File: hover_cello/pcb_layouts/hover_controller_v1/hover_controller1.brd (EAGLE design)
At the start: 160 x 100 mm, 6 parts

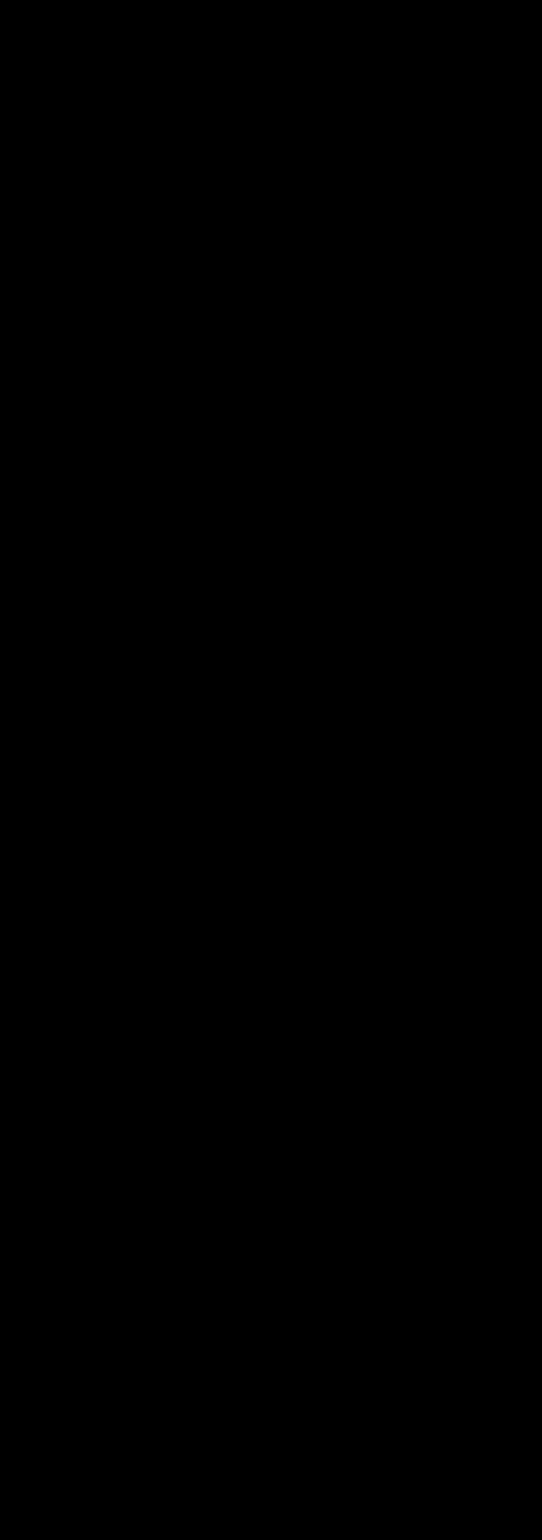
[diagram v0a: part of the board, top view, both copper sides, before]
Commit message: fixed annoying line not found bug, added delay on startup
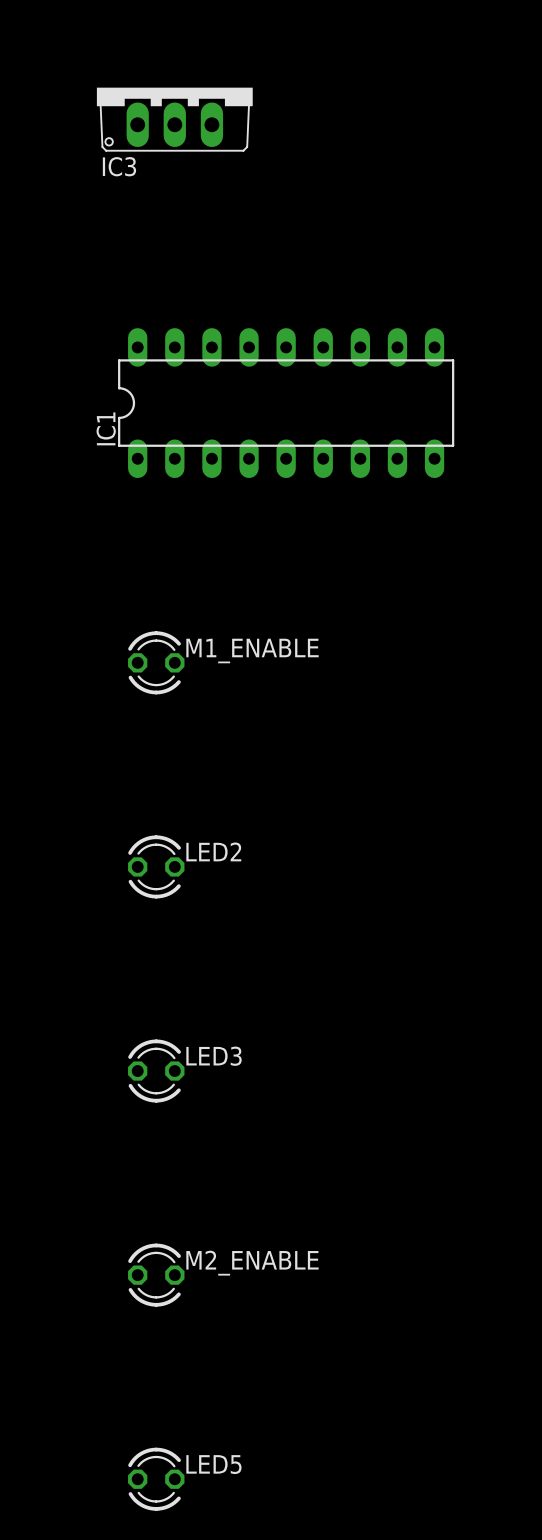
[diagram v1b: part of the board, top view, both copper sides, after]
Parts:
- added IC1: (no value), uln-udn:DIL18
- added IC3: 7805TV, linear:TO220V
- added LED2, LED3, LED5, M1_ENABLE, M2_ENABLE: (no value), led:LED3MM
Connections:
- new net N$3: LED3.K, M2_ENABLE.K
- new net N$4: LED3.A, M2_ENABLE.A
- net GND: now also IC1.9
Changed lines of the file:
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@@
 <element name="J1" library="jumper" package="SJW" value="" x="12.7" y="48.26" rot="R270"/>
 <element name="J2" library="jumper" package="SJW" value="" x="26.67" y="48.26" rot="R270"/>
+<element name="IC3" library="linear" package="TO220V" value="7805TV" x="10.16" y="-49.53"/>
+<element name="IC1" library="uln-udn" library_urn="urn:adsk.eagle:library:407" package="DIL18" value="" x="17.78" y="-71.12"/>
+<element name="M1_ENABLE" library="led" library_urn="urn:adsk.eagle:library:259" package="LED3MM" value="" x="8.89" y="-88.9"/>
+<element name="LED2" library="led" library_urn="urn:adsk.eagle:library:259" package="LED3MM" value="" x="8.89" y="-102.87"/>
+<element name="LED3" library="led" library_urn="urn:adsk.eagle:library:259" package="LED3MM" value="" x="8.89" y="-116.84"/>
+<element name="M2_ENABLE" library="led" library_urn="urn:adsk.eagle:library:259" package="LED3MM" value="" x="8.89" y="-130.81"/>
+<element name="LED5" library="led" library_urn="urn:adsk.eagle:library:259" package="LED3MM" value="" x="8.89" y="-144.78"/>
 </elements>
 <signals>
@@
 <contactref element="MOTOR2" pad="1"/>
 <contactref element="MOTOR1" pad="1"/>
+<contactref element="IC1" pad="9"/>
 <wire x1="12.7" y1="54.61" x2="26.67" y2="54.61" width="0" layer="19" extent="1-1"/>
 <wire x1="26.67" y1="34.671" x2="26.67" y2="54.61" width="0" layer="19" extent="1-1"/>
 <wire x1="39.37" y1="29.21" x2="26.67" y2="34.671" width="0" layer="19" extent="1-1"/>
 <wire x1="41.91" y1="29.21" x2="39.37" y2="29.21" width="0" layer="19" extent="1-1"/>
+<wire x1="27.94" y1="-74.93" x2="39.37" y2="29.21" width="0" layer="19" extent="1-1"/>
 </signal>
 <signal name="USB">
@@
 <wire x1="26.67" y1="24.511" x2="26.67" y2="59.69" width="0" layer="19" extent="1-1"/>
 </signal>
+<signal name="N$3">
+<contactref element="M2_ENABLE" pad="K"/>
+<contactref element="LED3" pad="K"/>
+<wire x1="10.16" y1="-116.84" x2="10.16" y2="-130.81" width="0" layer="19" extent="1-1"/>
+</signal>
+<signal name="N$4">
+<contactref element="M2_ENABLE" pad="A"/>
+<contactref element="LED3" pad="A"/>
+<wire x1="7.62" y1="-116.84" x2="7.62" y2="-130.81" width="0" layer="19" extent="1-1"/>
+</signal>
 </signals>
 </board>
 </drawing>
+<compatibility>
+<note version="8.2" severity="warning">
+Since Version 8.2, Eagle supports online libraries. The ids
+of those online libraries will not be understood (or retained)
+with this version.
+</note>
+</compatibility>
 </eagle>

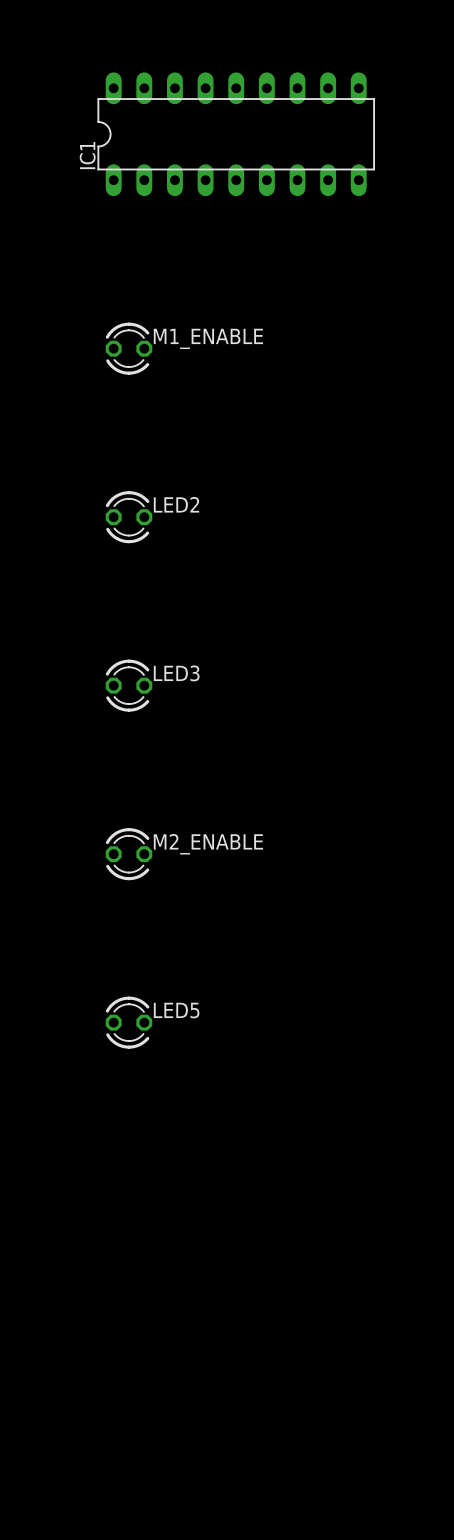
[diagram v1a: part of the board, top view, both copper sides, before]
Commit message: added L298 DC motor driver to Eagle schematic
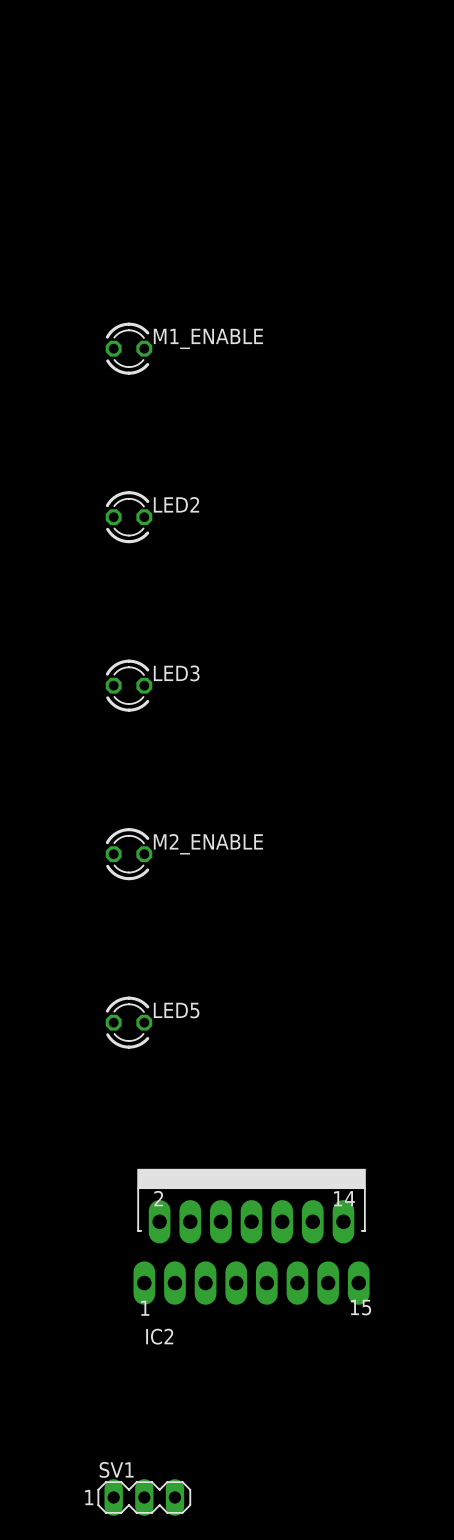
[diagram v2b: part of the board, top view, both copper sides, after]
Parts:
- removed IC1: (no value), uln-udn:DIL18
- added IC2: L298, st-microelectronics:MULTIWATT-15
- added SV1: (no value), con-lstb:MA03-1
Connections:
- new net VS: IC2.4
- net GND: now also IC2.8; no longer IC1.9
- net VCC: now also IC2.9
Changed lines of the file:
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@@
 <element name="J2" library="jumper" package="SJW" value="" x="26.67" y="48.26" rot="R270"/>
 <element name="IC3" library="linear" package="TO220V" value="7805TV" x="10.16" y="-49.53"/>
-<element name="IC1" library="uln-udn" library_urn="urn:adsk.eagle:library:407" package="DIL18" value="" x="17.78" y="-71.12"/>
 <element name="M1_ENABLE" library="led" library_urn="urn:adsk.eagle:library:259" package="LED3MM" value="" x="8.89" y="-88.9"/>
 <element name="LED2" library="led" library_urn="urn:adsk.eagle:library:259" package="LED3MM" value="" x="8.89" y="-102.87"/>
@@
 <element name="M2_ENABLE" library="led" library_urn="urn:adsk.eagle:library:259" package="LED3MM" value="" x="8.89" y="-130.81"/>
 <element name="LED5" library="led" library_urn="urn:adsk.eagle:library:259" package="LED3MM" value="" x="8.89" y="-144.78"/>
+<element name="IC2" library="st-microelectronics" package="MULTIWATT-15" value="L298" x="19.05" y="-158.75">
+<attribute name="MF" value="" x="19.05" y="-158.75" size="1.778" layer="27" display="off"/>
+<attribute name="MPN" value="L298N" x="19.05" y="-158.75" size="1.778" layer="27" display="off"/>
+<attribute name="OC_FARNELL" value="1589425" x="19.05" y="-158.75" size="1.778" layer="27" display="off"/>
+<attribute name="OC_NEWARK" value="32M1527" x="19.05" y="-158.75" size="1.778" layer="27" display="off"/>
+</element>
+<element name="SV1" library="con-lstb" package="MA03-1" value="" x="10.16" y="-184.15">
+<attribute name="MF" value="" x="10.16" y="-184.15" size="1.778" layer="27" display="off"/>
+<attribute name="MPN" value="" x="10.16" y="-184.15" size="1.778" layer="27" display="off"/>
+<attribute name="OC_FARNELL" value="unknown" x="10.16" y="-184.15" size="1.778" layer="27" display="off"/>
+<attribute name="OC_NEWARK" value="unknown" x="10.16" y="-184.15" size="1.778" layer="27" display="off"/>
+</element>
 </elements>
 <signals>
@@
 <contactref element="MOTOR2" pad="1"/>
 <contactref element="MOTOR1" pad="1"/>
-<contactref element="IC1" pad="9"/>
+<contactref element="IC2" pad="8"/>
+<wire x1="39.37" y1="29.21" x2="19.05" y2="-161.29" width="0" layer="19" extent="1-1"/>
+<wire x1="41.91" y1="29.21" x2="39.37" y2="29.21" width="0" layer="19" extent="1-1"/>
+<wire x1="26.67" y1="34.671" x2="39.37" y2="29.21" width="0" layer="19" extent="1-1"/>
+<wire x1="26.67" y1="54.61" x2="26.67" y2="34.671" width="0" layer="19" extent="1-1"/>
 <wire x1="12.7" y1="54.61" x2="26.67" y2="54.61" width="0" layer="19" extent="1-1"/>
-<wire x1="26.67" y1="34.671" x2="26.67" y2="54.61" width="0" layer="19" extent="1-1"/>
-<wire x1="39.37" y1="29.21" x2="26.67" y2="34.671" width="0" layer="19" extent="1-1"/>
-<wire x1="41.91" y1="29.21" x2="39.37" y2="29.21" width="0" layer="19" extent="1-1"/>
-<wire x1="27.94" y1="-74.93" x2="39.37" y2="29.21" width="0" layer="19" extent="1-1"/>
 </signal>
 <signal name="USB">
@@
 <contactref element="J2" pad="2"/>
 <contactref element="U$1" pad="VCC"/>
-<wire x1="39.37" y1="31.75" x2="41.91" y2="31.75" width="0" layer="19" extent="1-1"/>
-<wire x1="26.67" y1="29.591" x2="39.37" y2="31.75" width="0" layer="19" extent="1-1"/>
+<contactref element="IC2" pad="9"/>
+<wire x1="26.67" y1="29.591" x2="20.32" y2="-166.37" width="0" layer="19" extent="1-1"/>
+<wire x1="39.37" y1="31.75" x2="26.67" y2="29.591" width="0" layer="19" extent="1-1"/>
+<wire x1="41.91" y1="31.75" x2="39.37" y2="31.75" width="0" layer="19" extent="1-1"/>
 <wire x1="26.67" y1="46.99" x2="26.67" y2="29.591" width="0" layer="19" extent="1-1"/>
 <wire x1="12.7" y1="46.99" x2="26.67" y2="46.99" width="0" layer="19" extent="1-1"/>
@@
 <wire x1="7.62" y1="-116.84" x2="7.62" y2="-130.81" width="0" layer="19" extent="1-1"/>
 </signal>
+<signal name="VS">
+<contactref element="IC2" pad="4"/>
+</signal>
 </signals>

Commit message: wrote basic thermal data visualizer in processing for D6T
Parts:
- removed J1, J2: (no value), jumper:SJW
- removed LED2, LED3, LED5, M1_ENABLE, M2_ENABLE: (no value), led:LED3MM
- removed MOTOR1, MOTOR2: (no value), GeekAmmo:06X1-PTH
- added D1, D2, D3, D4, D5, D6, D7, D8: (no value), diode:DO35-7
- added VR1, VR2: (no value), MusicThingModular:BOURNS_3362P_TRIMMER
- moved IC2 238.6 mm to (67.3, 74.9)
- moved SV1 238.6 mm to (58.4, 49.5)
- moved IC3 66.6 mm to (44.5, 7.62)
- moved U$1 5.39 mm to (22.9, 17.8)
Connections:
- removed net M1_DIRECTION: MOTOR1.3, U$1.4
- removed net M1_ENABLE: MOTOR1.5, U$1.3
- removed net M2_DIRECTION: MOTOR2.3, U$1.6
- removed net M2_ENABLE: MOTOR2.5, U$1.5
- removed net VS: IC2.4
- new net +18V: IC2.4, IC3.1
- new net EN_A: IC2.6, U$1.9
- new net EN_B: IC2.11, U$1.10
- new net N$5: U$1.A3, VR2.2
- new net N$6: U$1.A2, VR1.2
- net GND: now also IC3.2, VR1.1, VR2.1; no longer MOTOR1.1, MOTOR2.1
- net N$1: now also IC2.5, U$1.3; no longer J1.1, MOTOR1.6
- net N$2: now also IC2.7, U$1.4; no longer J2.1, MOTOR2.6
- net N$3: now also IC2.10, U$1.5; no longer LED3.K, M2_ENABLE.K
- net N$4: now also IC2.12, U$1.6; no longer LED3.A, M2_ENABLE.A
- net VCC: now also IC3.3, VR1.3, VR2.3; no longer J1.2, J2.2
